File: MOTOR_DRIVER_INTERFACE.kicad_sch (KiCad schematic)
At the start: 6 parts, among them J10 DRV_HIGH_C2, J11 DRV_LOW_C2, J12 DRV_HIGH_C3, J13 DRV_LOW_C3, J14 DRV_LOW_C1, J9 DRV_HIGH_C1

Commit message: board layout v1
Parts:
- added D2, D4, D5, D6: LED, LED_SMD:LED_1206_3216Metric_Pad1.42x1.75mm_HandSolder, symbol Device:LED
- added K1, K2, K3, K5: RAYEX-L90, Relay_THT:Relay_SPDT_RAYEX-L90, symbol Relay:RAYEX-L90
- added R25, R26, R27, R28: 10k, Resistor_SMD:R_1206_3216Metric, symbol Device:R_US
- added U3: 74AHC1G08, Package_TO_SOT_SMD:SOT-23-5_HandSoldering, symbol 74xGxx:74AHC1G08
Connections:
- net RX_LOW_5v is gone; now on net RX_DRV_5v: J14.7 (Pin_7)
- net 5v_reg_HIGH: no longer J9.9 (Pin_9)
- net 5v_reg_LOW: no longer J14.9 (Pin_9)
- net GND: now also D2.1 (K), D4.1 (K), D5.1 (K), D6.1 (K), K1.14, K1.A1, K2.A1, K3.12, K3.A1, K5.A1, U3.3 (GND)
- net ERR_HIGH renamed ERR_STR
- net ERR_STR: now also R26.1
- net ERR_LOW renamed ERR_BRK
- net ERR_BRK: now also R28.1
- net RX_HIGH_5v renamed RX_DRV_5v
- net TX_HIGH_5v renamed TX_STR_5v
- net TX_STR_5v: now also U3.2
- net TX_LOW_5v renamed TX_BRK_5v
- net TX_BRK_5v: now also U3.1
- net ~{RST_HIGH} renamed ~{RST_STR}
- net ~{RST_LOW} renamed ~{RST_BRK}
- new net: K1.12, K5.11A, K5.11B
- new net: K2.12, K3.11A, K3.11B
- new net: D6.2 (A), R28.2
- new net: D4.2 (A), R26.2
- new net: D5.2 (A), R27.2
- new net: D2.2 (A), R25.2
- new net +12V_BRK: K2.14, K5.12
- new net +5V: U3.5 (VCC)
- new net 5v_reg_BRK: J14.9 (Pin_9), R27.1
- new net 5v_reg_STR: J9.9 (Pin_9), R25.1
- new net BRK_+: K1.11A, K1.11B
- new net BRK_-: K2.11A, K2.11B
- new net BRK_CTRL_+: K5.14
- new net BRK_CTRL_-: K3.14
- new net BRK_RELEASE: K1.A2, K2.A2
- new net TX_DRV_5v: U3.4
- new net ~{E-STOP}: K3.A2, K5.A2
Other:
- title: (none) -> AAV edge motor controller
- moved on the sheet: J10, J11, J12, J13, J14, J9

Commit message: Review and fixes from reliability and safety team
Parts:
- added C11: 0.1uF, Capacitor_SMD:C_1206_3216Metric, symbol Device:C_Small
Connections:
- net +5V: now also C11.1
- net GND: now also C11.2
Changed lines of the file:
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@@
+	)
+	(junction
+		(at 55.88 100.33)
+		(diameter 0)
+		(color 0 0 0 0)
 	)
 	(junction
@@
 	)
 	(junction
+		(at 55.88 120.65)
+		(diameter 0)
+		(color 0 0 0 0)
+	)
+	(junction
 		(at 83.82 34.29)
 		(diameter 0)
@@
 	(wire
 		(pts
+			(xy 93.98 100.33) (xy 93.98 107.95)
+		)
+		(stroke
+			(width 0)
+			(type default)
+		)
+	)
+	(wire
+		(pts
 			(xy 207.01 41.91) (xy 207.01 36.83)
 		)
@@
 	(wire
 		(pts
+			(xy 93.98 120.65) (xy 93.98 113.03)
+		)
+		(stroke
+			(width 0)
+			(type default)
+		)
+	)
+	(wire
+		(pts
 			(xy 35.56 107.95) (xy 40.64 107.95)
 		)
@@
 	(wire
 		(pts
+			(xy 55.88 120.65) (xy 93.98 120.65)
+		)
+		(stroke
+			(width 0)
+			(type default)
+		)
+	)
+	(wire
+		(pts
 			(xy 173.99 71.12) (xy 177.8 71.12)
 		)
@@
 		(pts
 			(xy 59.69 63.5) (xy 59.69 62.23)
+		)
+		(stroke
+			(width 0)
+			(type default)
+		)
+	)
+	(wire
+		(pts
+			(xy 55.88 100.33) (xy 93.98 100.33)
 		)
 		(stroke
@@
 			)
 		)
+	)
+	(symbol
+		(lib_id "Device:C_Small")
+		(at 93.98 110.49 0)
+		(unit 1)
+		(exclude_from_sim no)
+		(in_bom yes)
+		(on_board yes)
+		(dnp no)
+		(property "Reference" "C11"
+			(at 89.916 112.014 0)
+			(effects
+				(font
+					(size 1.27 1.27)
+				)
+				(justify left)
+			)
+		)
+		(property "Value" "0.1uF"
+			(at 87.884 105.41 0)
+			(effects
+				(font
+					(size 1.27 1.27)
+				)
+				(justify left)
+			)
+		)
+		(property "Footprint" "Capacitor_SMD:C_1206_3216Metric"
+			(at 93.98 110.49 0)
+			(effects
+				(font
+					(size 1.27 1.27)
+				)
+				(hide yes)
+			)
+		)
+		(property "Datasheet" "~"
+			(at 93.98 110.49 0)
+			(effects
+				(font
+					(size 1.27 1.27)
+				)
+				(hide yes)
+			)
+		)
+		(property "Description" "Unpolarized capacitor, small symbol"
+			(at 93.98 110.49 0)
+			(effects
+				(font
+					(size 1.27 1.27)
+				)
+				(hide yes)
+			)
+		)
+		(pin "1"
+		)
+		(pin "2"
+		)
+		(instances
+			(project "AAV_embedded"
+				(path "/00c590f3-503a-497c-946e-4acf8f8302df/a133e678-5368-4dc9-bd48-fd90f9bfdabc"
+					(reference "C11")
+					(unit 1)
+				)
+			)
+		)

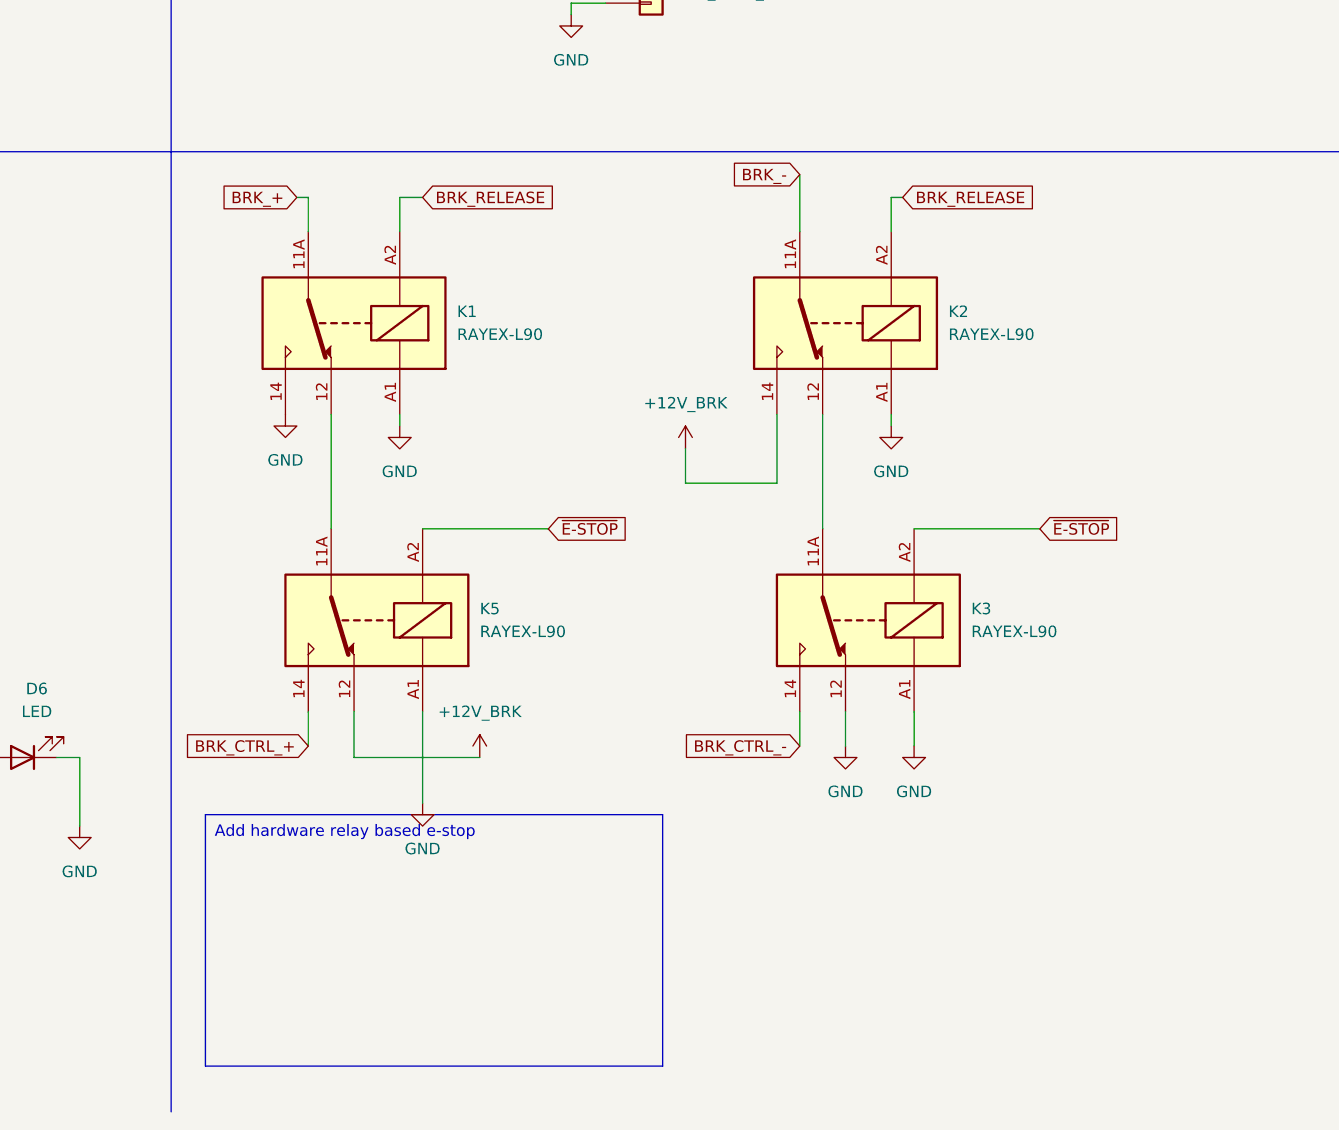
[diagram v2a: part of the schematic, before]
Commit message: added micromod breakout and fixed voltage divider
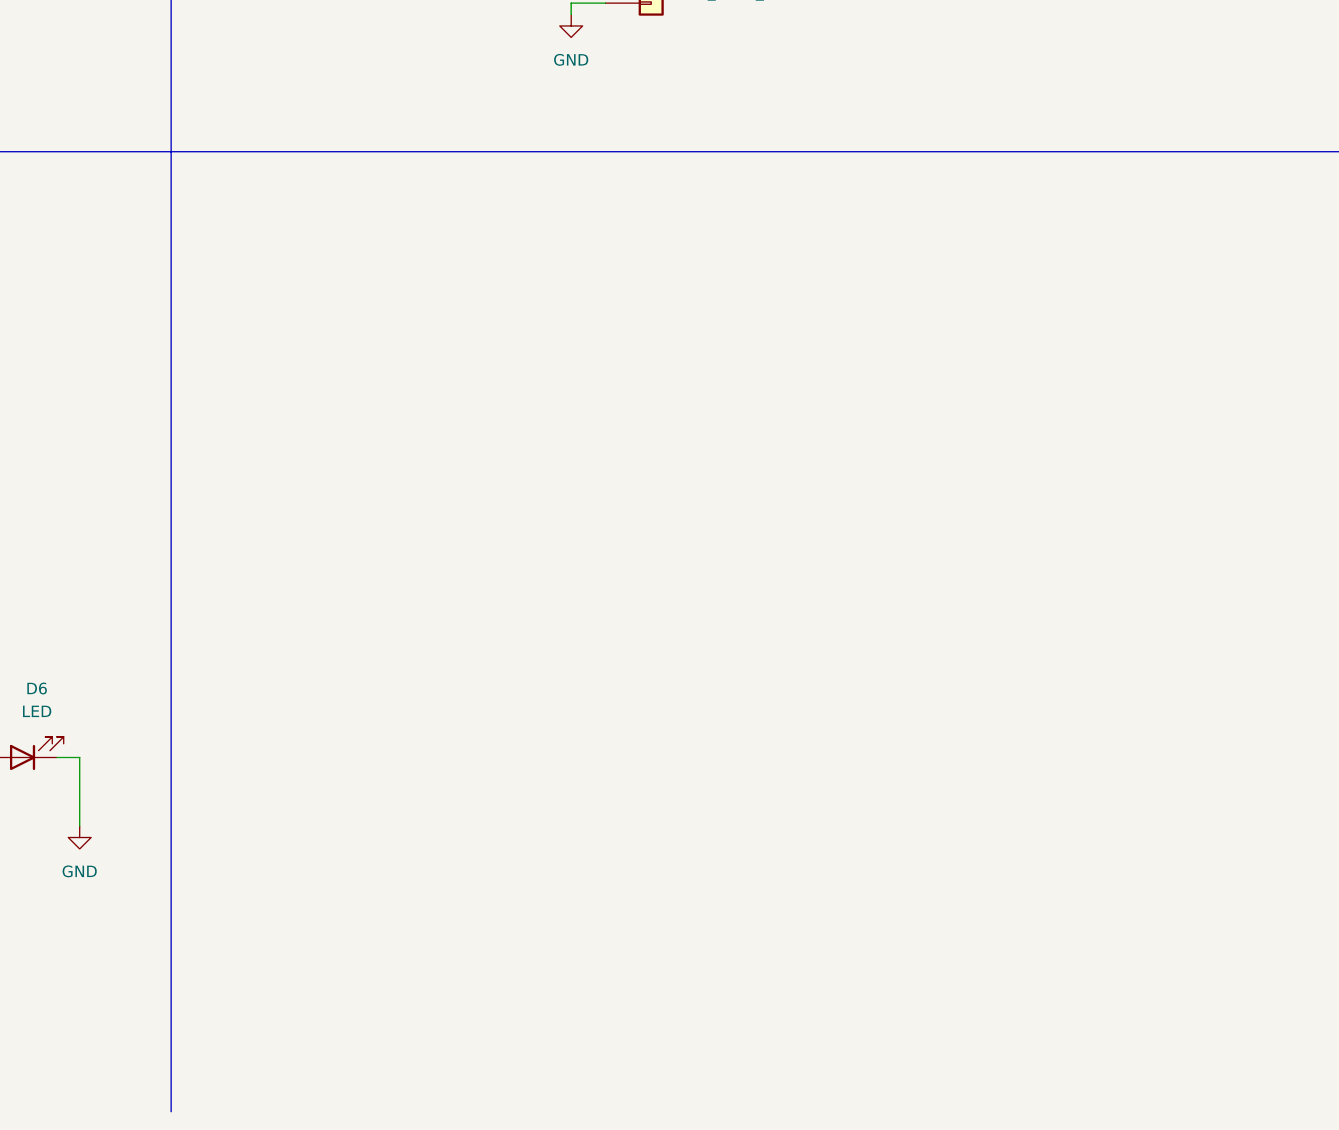
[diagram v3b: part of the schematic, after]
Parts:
- removed K1, K2, K3, K5: RAYEX-L90, Relay_THT:Relay_SPDT_RAYEX-L90, symbol Relay:RAYEX-L90
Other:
- company: (none) -> Charlie Wadds

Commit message: changed LED
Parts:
- D2, D4, D5, D6: footprint LED_SMD:LED_1206_3216Metric_Pad1.42x1.75mm_HandSolder -> LED_SMD:LED_0805_2012Metric
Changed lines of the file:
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@@
 			)
 		)
-		(property "Footprint" "LED_SMD:LED_1206_3216Metric_Pad1.42x1.75mm_HandSolder"
+		(property "Footprint" "LED_SMD:LED_0805_2012Metric"
 			(at 55.88 157.48 0)
 			(effects
@@
 			)
 		)
-		(property "Footprint" "LED_SMD:LED_1206_3216Metric_Pad1.42x1.75mm_HandSolder"
+		(property "Footprint" "LED_SMD:LED_0805_2012Metric"
 			(at 90.17 158.75 0)
 			(effects
@@
 			)
 		)
-		(property "Footprint" "LED_SMD:LED_1206_3216Metric_Pad1.42x1.75mm_HandSolder"
+		(property "Footprint" "LED_SMD:LED_0805_2012Metric"
 			(at 113.03 158.75 0)
 			(effects
@@
 			)
 		)
-		(property "Footprint" "LED_SMD:LED_1206_3216Metric_Pad1.42x1.75mm_HandSolder"
+		(property "Footprint" "LED_SMD:LED_0805_2012Metric"
 			(at 34.29 157.48 0)
 			(effects
